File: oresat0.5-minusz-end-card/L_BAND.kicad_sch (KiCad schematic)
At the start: 1 part

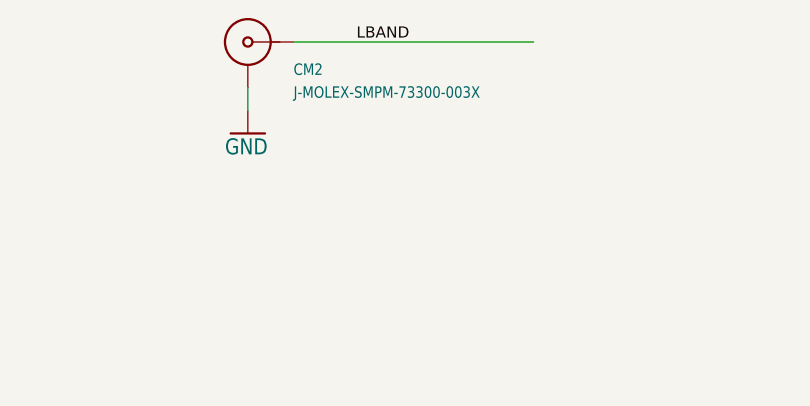
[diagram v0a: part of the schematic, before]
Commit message: Updated -Z end card and replaced eagle imported libraries with kicad libraries
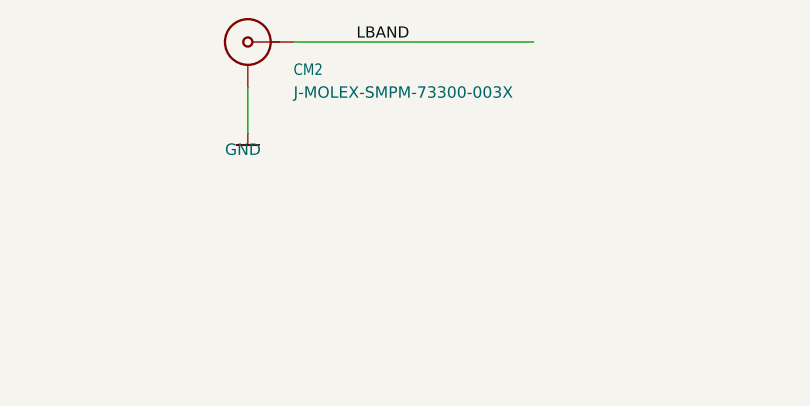
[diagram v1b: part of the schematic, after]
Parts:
- CM2: footprint oresat-footprints:J-MOLEX-SMPM-073300-003X -> oresat-connectors:J-MOLEX-SMPM-073300-003X; symbol OreSat-j-molex-smpm-73300-003x:J-MOLEX-SMPM-73300-003X -> oresat-connectors:J-MOLEX-SMPM-73300-003X
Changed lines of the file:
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@@
     (rev "1.0")
   )
-  (wire (pts (xy 54.61 109.22) (xy 54.61 106.68))
+  (wire (pts (xy 54.61 106.68) (xy 54.61 111.76))
     (stroke (width 0) (type default) (color 0 0 0 0))
   )
@@
     (effects (font (size 1.2446 1.2446)) (justify left bottom))
   )
-  (symbol (lib_id "OreSat-j-molex-smpm-73300-003x:J-MOLEX-SMPM-73300-003X") (at 54.61 101.6 0) (unit 1)
+  (symbol (lib_id "oresat-connectors:J-MOLEX-SMPM-73300-003X") (at 54.61 101.6 0) (unit 1)
     (in_bom yes) (on_board yes)
     (property "Reference" "CM2" (id 0) (at 59.69 105.41 0)
@@
     )
     (property "Value" "J-MOLEX-SMPM-73300-003X" (id 1) (at 59.69 107.95 0)
-      (effects (font (size 1.27 1.0795)) (justify left bottom))
+      (effects (font (size 1.27 1.27)) (justify left bottom))
     )
-    (property "Footprint" "oresat-footprints:J-MOLEX-SMPM-073300-003X" (id 2) (at 54.61 101.6 0)
+    (property "Footprint" "oresat-connectors:J-MOLEX-SMPM-073300-003X" (id 2) (at 54.61 101.6 0)
       (effects (font (size 1.27 1.27)) hide)
     )
@@
     (pin "RF")
   )
-  (symbol (lib_id "plusz-end-card-with-turnstile-eagle-import:GND") (at 54.61 111.76 0) (unit 1)
+  (symbol (lib_id "oresat-power:GND") (at 54.61 111.76 0) (unit 1)
     (in_bom yes) (on_board yes)
     (property "Reference" "#GND010" (id 0) (at 54.61 111.76 0)
@@
     )
     (property "Value" "GND" (id 1) (at 52.07 114.3 0)
-      (effects (font (size 1.778 1.5113)) (justify left bottom))
+      (effects (font (size 1.27 1.27)) (justify left bottom))
     )
     (property "Footprint" "plusz-end-card-with-turnstile:" (id 2) (at 54.61 111.76 0)

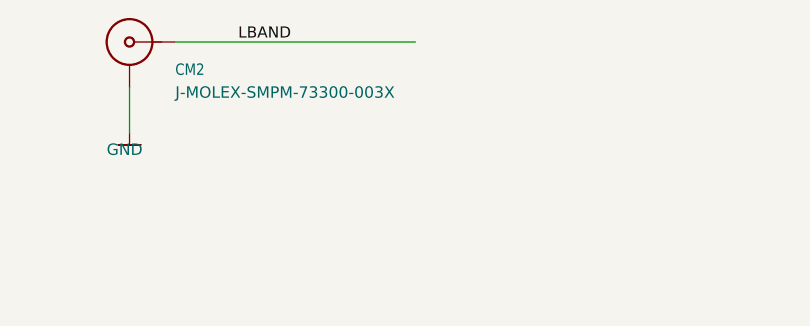
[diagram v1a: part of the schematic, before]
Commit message: -Z end card design review changes, and added antenna feeds
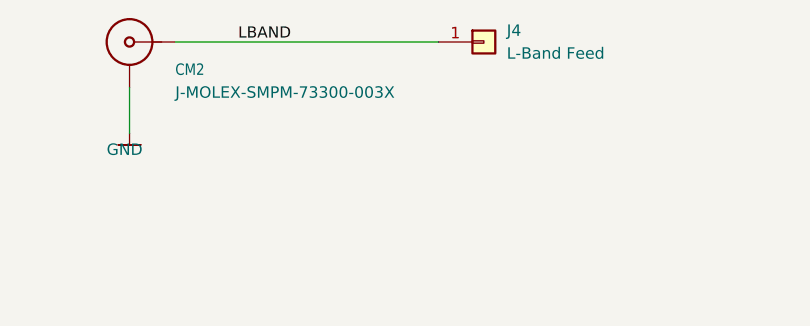
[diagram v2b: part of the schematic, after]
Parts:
- added J4: L-Band Feed, Connector_Pin:Pin_D1.0mm_L10.0mm, symbol Connector_Generic:Conn_01x01
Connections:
- net LBAND: now also J4.1 (Pin_1)
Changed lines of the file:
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@@
     (stroke (width 0) (type default) (color 0 0 0 0))
   )
-  (wire (pts (xy 59.69 101.6) (xy 86.36 101.6))
+  (wire (pts (xy 59.69 101.6) (xy 88.9 101.6))
     (stroke (width 0) (type default) (color 0 0 0 0))
   )
@@
     (pin "RF")
   )
+  (symbol (lib_id "Connector_Generic:Conn_01x01") (at 93.98 101.6 0) (unit 1)
+    (in_bom yes) (on_board yes) (fields_autoplaced)
+    (property "Reference" "J4" (id 0) (at 96.52 100.3299 0)
+      (effects (font (size 1.27 1.27)) (justify left))
+    )
+    (property "Value" "L-Band Feed" (id 1) (at 96.52 102.8699 0)
+      (effects (font (size 1.27 1.27)) (justify left))
+    )
+    (property "Footprint" "Connector_Pin:Pin_D1.0mm_L10.0mm" (id 2) (at 93.98 101.6 0)
+      (effects (font (size 1.27 1.27)) hide)
+    )
+    (property "Datasheet" "~" (id 3) (at 93.98 101.6 0)
+      (effects (font (size 1.27 1.27)) hide)
+    )
+    (pin "1")
+  )
   (symbol (lib_id "oresat-power:GND") (at 54.61 111.76 0) (unit 1)

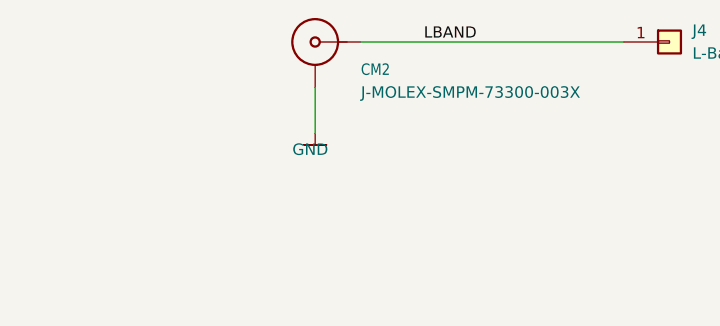
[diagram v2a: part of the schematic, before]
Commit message: Updated OreSat 0.5 end card board outlines and mounting holes, and fixed KiCad library warnings
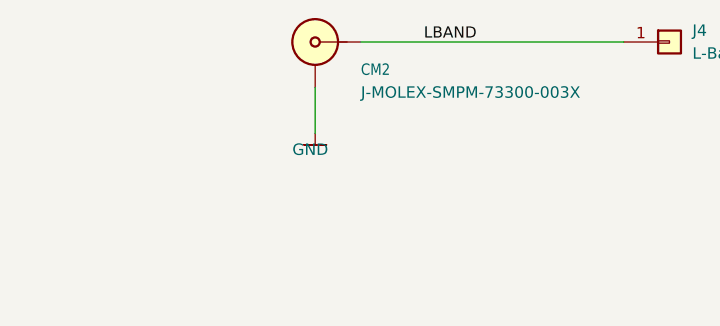
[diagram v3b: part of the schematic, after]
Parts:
- CM2: footprint oresat-connectors:J-MOLEX-SMPM-073300-003X -> oresat-connectors:J-MOLEX-SMPM-073300-002X; symbol oresat-connectors:J-MOLEX-SMPM-73300-003X -> oresat-connectors:J-MOLEX-SMPM-73300-002X
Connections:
- net GND: now also CM2.SHLD; no longer CM2.GND (SHIELD3)
- net LBAND: now also CM2.SIG; no longer CM2.RF (CENTER)
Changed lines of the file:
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@@
-(kicad_sch (version 20211123) (generator eeschema)
+(kicad_sch (version 20230121) (generator eeschema)
   (paper "USLedger")
   (title_block
@@
   )
   (wire (pts (xy 54.61 106.68) (xy 54.61 111.76))
-    (stroke (width 0) (type default) (color 0 0 0 0))
+    (stroke (width 0) (type default))
   )
   (wire (pts (xy 59.69 101.6) (xy 88.9 101.6))
-    (stroke (width 0) (type default) (color 0 0 0 0))
+    (stroke (width 0) (type default))
   )
-  (text "L Band Feed System (1.265 GHz)" (at 21.59 247.65 180)
+  (text "L Band Feed System (1.265 GHz)" (at 21.59 247.65 0)
     (effects (font (size 4.572 3.8862)) (justify left bottom))
   )
-  (label "LBAND" (at 66.675 101.6 0)
+  (label "LBAND" (at 66.675 101.6 0) (fields_autoplaced)
     (effects (font (size 1.2446 1.2446)) (justify left bottom))
   )
-  (symbol (lib_id "oresat-connectors:J-MOLEX-SMPM-73300-003X") (at 54.61 101.6 0) (unit 1)
-    (in_bom yes) (on_board yes)
-    (property "Reference" "CM2" (id 0) (at 59.69 105.41 0)
+  (symbol (lib_id "oresat-connectors:J-MOLEX-SMPM-73300-002X") (at 54.61 101.6 0) (unit 1)
+    (in_bom yes) (on_board yes) (dnp no)
+    (property "Reference" "CM2" (at 59.69 105.41 0)
       (effects (font (size 1.27 1.0795)) (justify left bottom))
     )
-    (property "Value" "J-MOLEX-SMPM-73300-003X" (id 1) (at 59.69 107.95 0)
+    (property "Value" "J-MOLEX-SMPM-73300-003X" (at 59.69 107.95 0)
       (effects (font (size 1.27 1.27)) (justify left bottom))
     )
-    (property "Footprint" "oresat-connectors:J-MOLEX-SMPM-073300-003X" (id 2) (at 54.61 101.6 0)
+    (property "Footprint" "oresat-connectors:J-MOLEX-SMPM-073300-002X" (at 54.61 95.25 0)
       (effects (font (size 1.27 1.27)) hide)
     )
-    (property "Datasheet" "" (id 3) (at 54.61 101.6 0)
+    (property "Datasheet" "https://tools.molex.com/pdm_docs/sd/733000020_sd.pdf" (at 54.61 92.71 0)
       (effects (font (size 1.27 1.27)) hide)
     )
-    (pin "GND")
-    (pin "RF")
+    (pin "SHLD")
+    (pin "SIG")
+    (instances
+      (project "oresat0.5-minusz-end-card"
+        (path "/f7595184-4323-4ed9-b19e-5e32e3c6e76f/e6c8a025-92ad-43ea-8ca0-148adc1f93f0"
+          (reference "CM2") (unit 1)
+        )
+      )
+    )
   )
   (symbol (lib_id "Connector_Generic:Conn_01x01") (at 93.98 101.6 0) (unit 1)
-    (in_bom yes) (on_board yes) (fields_autoplaced)
-    (property "Reference" "J4" (id 0) (at 96.52 100.3299 0)
+    (in_bom yes) (on_board yes) (dnp no) (fields_autoplaced)
+    (property "Reference" "J4" (at 96.52 100.3299 0)
       (effects (font (size 1.27 1.27)) (justify left))
     )
-    (property "Value" "L-Band Feed" (id 1) (at 96.52 102.8699 0)
+    (property "Value" "L-Band Feed" (at 96.52 102.8699 0)
       (effects (font (size 1.27 1.27)) (justify left))
     )
-    (property "Footprint" "Connector_Pin:Pin_D1.0mm_L10.0mm" (id 2) (at 93.98 101.6 0)
+    (property "Footprint" "Connector_Pin:Pin_D1.0mm_L10.0mm" (at 93.98 101.6 0)
       (effects (font (size 1.27 1.27)) hide)
     )
-    (property "Datasheet" "~" (id 3) (at 93.98 101.6 0)
+    (property "Datasheet" "~" (at 93.98 101.6 0)
       (effects (font (size 1.27 1.27)) hide)
     )
     (pin "1")
+    (instances
+      (project "oresat0.5-minusz-end-card"
+        (path "/f7595184-4323-4ed9-b19e-5e32e3c6e76f/e6c8a025-92ad-43ea-8ca0-148adc1f93f0"
+          (reference "J4") (unit 1)
+        )
+      )
+    )
   )
   (symbol (lib_id "oresat-power:GND") (at 54.61 111.76 0) (unit 1)
-    (in_bom yes) (on_board yes)
-    (property "Reference" "#GND010" (id 0) (at 54.61 111.76 0)
+    (in_bom yes) (on_board yes) (dnp no)
+    (property "Reference" "#GND010" (at 54.61 111.76 0)
       (effects (font (size 1.27 1.27)) hide)
     )
-    (property "Value" "GND" (id 1) (at 52.07 114.3 0)
+    (property "Value" "GND" (at 52.07 114.3 0)
       (effects (font (size 1.27 1.27)) (justify left bottom))
     )
-    (property "Footprint" "plusz-end-card-with-turnstile:" (id 2) (at 54.61 111.76 0)
+    (property "Footprint" "plusz-end-card-with-turnstile:" (at 54.61 111.76 0)
       (effects (font (size 1.27 1.27)) hide)
     )
-    (property "Datasheet" "" (id 3) (at 54.61 111.76 0)
+    (property "Datasheet" "" (at 54.61 111.76 0)
       (effects (font (size 1.27 1.27)) hide)
     )
     (pin "1")
+    (instances
+      (project "oresat0.5-minusz-end-card"
+        (path "/f7595184-4323-4ed9-b19e-5e32e3c6e76f/e6c8a025-92ad-43ea-8ca0-148adc1f93f0"
+          (reference "#GND010") (unit 1)
+        )
+      )
+    )
   )
 )

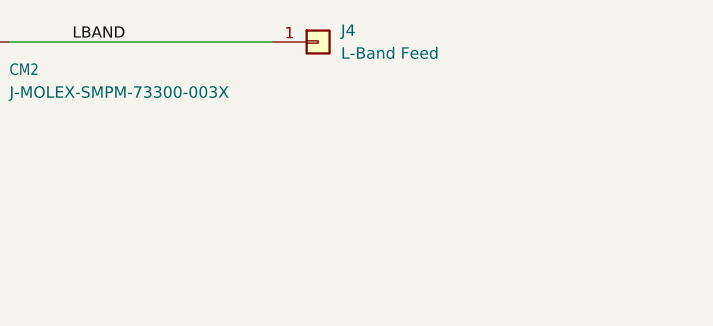
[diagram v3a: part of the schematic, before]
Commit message: Updated -Z end card and DXF
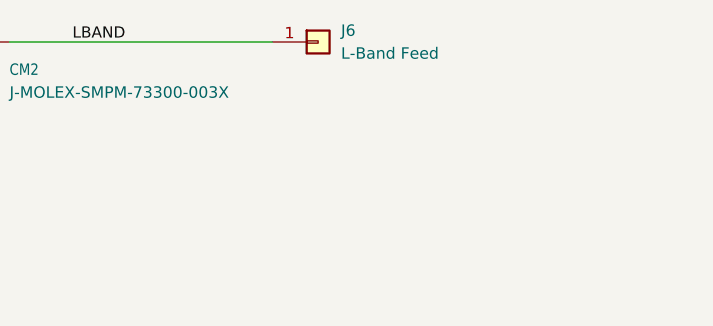
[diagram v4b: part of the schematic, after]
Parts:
- renumbered J4 to J6
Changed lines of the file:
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@@
   (symbol (lib_id "Connector_Generic:Conn_01x01") (at 93.98 101.6 0) (unit 1)
     (in_bom yes) (on_board yes) (dnp no) (fields_autoplaced)
-    (property "Reference" "J4" (at 96.52 100.3299 0)
+    (property "Reference" "J6" (at 96.52 100.33 0)
       (effects (font (size 1.27 1.27)) (justify left))
     )
-    (property "Value" "L-Band Feed" (at 96.52 102.8699 0)
+    (property "Value" "L-Band Feed" (at 96.52 102.87 0)
       (effects (font (size 1.27 1.27)) (justify left))
     )
@@
       (project "oresat0.5-minusz-end-card"
         (path "/f7595184-4323-4ed9-b19e-5e32e3c6e76f/e6c8a025-92ad-43ea-8ca0-148adc1f93f0"
-          (reference "J4") (unit 1)
+          (reference "J6") (unit 1)
         )
       )
